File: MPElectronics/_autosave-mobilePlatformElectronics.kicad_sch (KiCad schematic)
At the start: 94 parts, among them J1 UART, J2 UART, J3 Magnetic Encoder, J4 Magnetic Encoder, M1 Motor_DC, M2 Motor_DC, M3 Motor_DC, M4 Motor_DC, M5 SG90 9g Micro Servo, M6 RDS51150, M7 RDS51150, M8 SY35ST28-0504A_Stepper_Motor_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, Q1 LTR3208E, SW1 Reset, SW2 Reset, SW3 Reset, SW4 SW_SPDT, SW6 SW_SPDT_LIMIT, SW7 SW_SPDT_LIMIT, U1 PIC32MX170F256B, U10 TLE5206-2S, U12 IR Distance, U13 IR Distance, U14 L293NE/SN754410NE, U2 TLE5206-2S, U3 PIC32MX170F256B, U4 IR Line Sensor, U5 IR Line Sensor, U6 IR Line Sensor, U7 MCP6294, U8 MCP6546, U9 IR Line Sensor

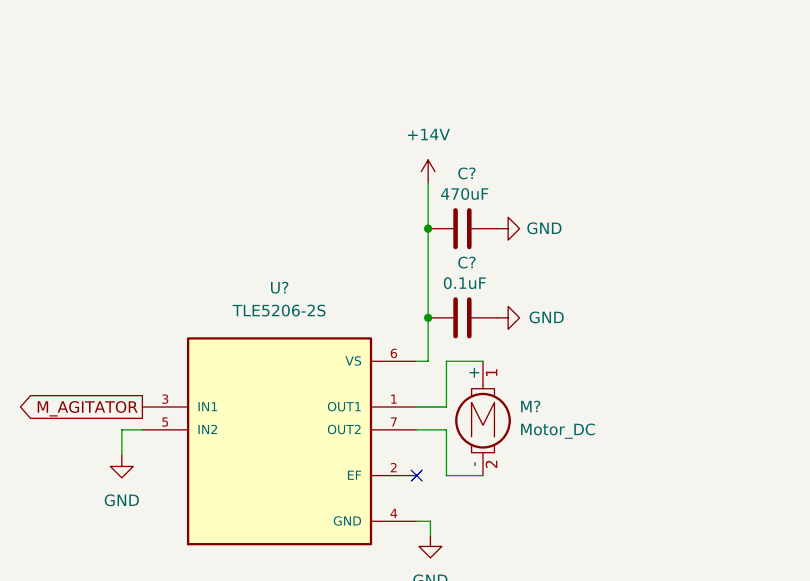
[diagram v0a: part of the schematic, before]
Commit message: structurally complete operator code V1 including agitator and intake controlled by OperatorFSM
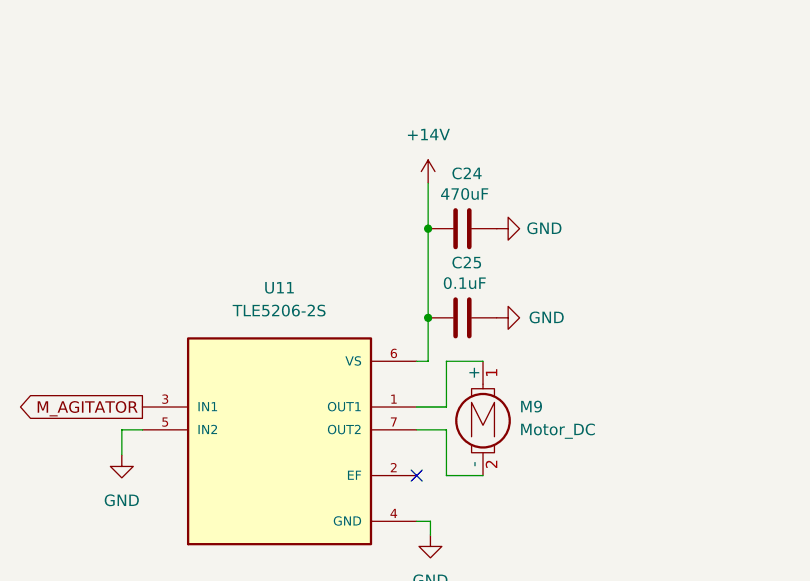
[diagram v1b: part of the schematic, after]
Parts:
- gave numbers to parts that had none: 4
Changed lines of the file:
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@@
 		(dnp no)
 		(fields_autoplaced yes)
-		(property "Reference" "M?"
+		(property "Reference" "M9"
 			(at 356.616 489.9659 0)
 			(effects
@@
 			(project "mobilePlatformElectronics"
 				(path "/bd24c4db-4e36-4117-bd4f-5228ef241da9"
-					(reference "M?")
+					(reference "M9")
 					(unit 1)
 				)
@@
 		(on_board yes)
 		(dnp no)
-		(property "Reference" "C?"
+		(property "Reference" "C25"
 			(at 350.774 473.964 90)
 			(effects
@@
 			(project "mobilePlatformElectronics"
 				(path "/bd24c4db-4e36-4117-bd4f-5228ef241da9"
-					(reference "C?")
+					(reference "C25")
 					(unit 1)
 				)
@@
 		(on_board yes)
 		(dnp no)
-		(property "Reference" "C?"
+		(property "Reference" "C24"
 			(at 350.774 464.058 90)
 			(effects
@@
 			(project "mobilePlatformElectronics"
 				(path "/bd24c4db-4e36-4117-bd4f-5228ef241da9"
-					(reference "C?")
+					(reference "C24")
 					(unit 1)
 				)
@@
 		(dnp no)
 		(fields_autoplaced yes)
-		(property "Reference" "U?"
+		(property "Reference" "U11"
 			(at 329.946 476.758 0)
 			(effects
@@
 			(project "mobilePlatformElectronics"
 				(path "/bd24c4db-4e36-4117-bd4f-5228ef241da9"
-					(reference "U?")
+					(reference "U11")
 					(unit 1)
 				)
